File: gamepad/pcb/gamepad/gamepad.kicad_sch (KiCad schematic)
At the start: 11 parts, among them U1 Pico, U2 ADC, U3 RP2040-ZERO

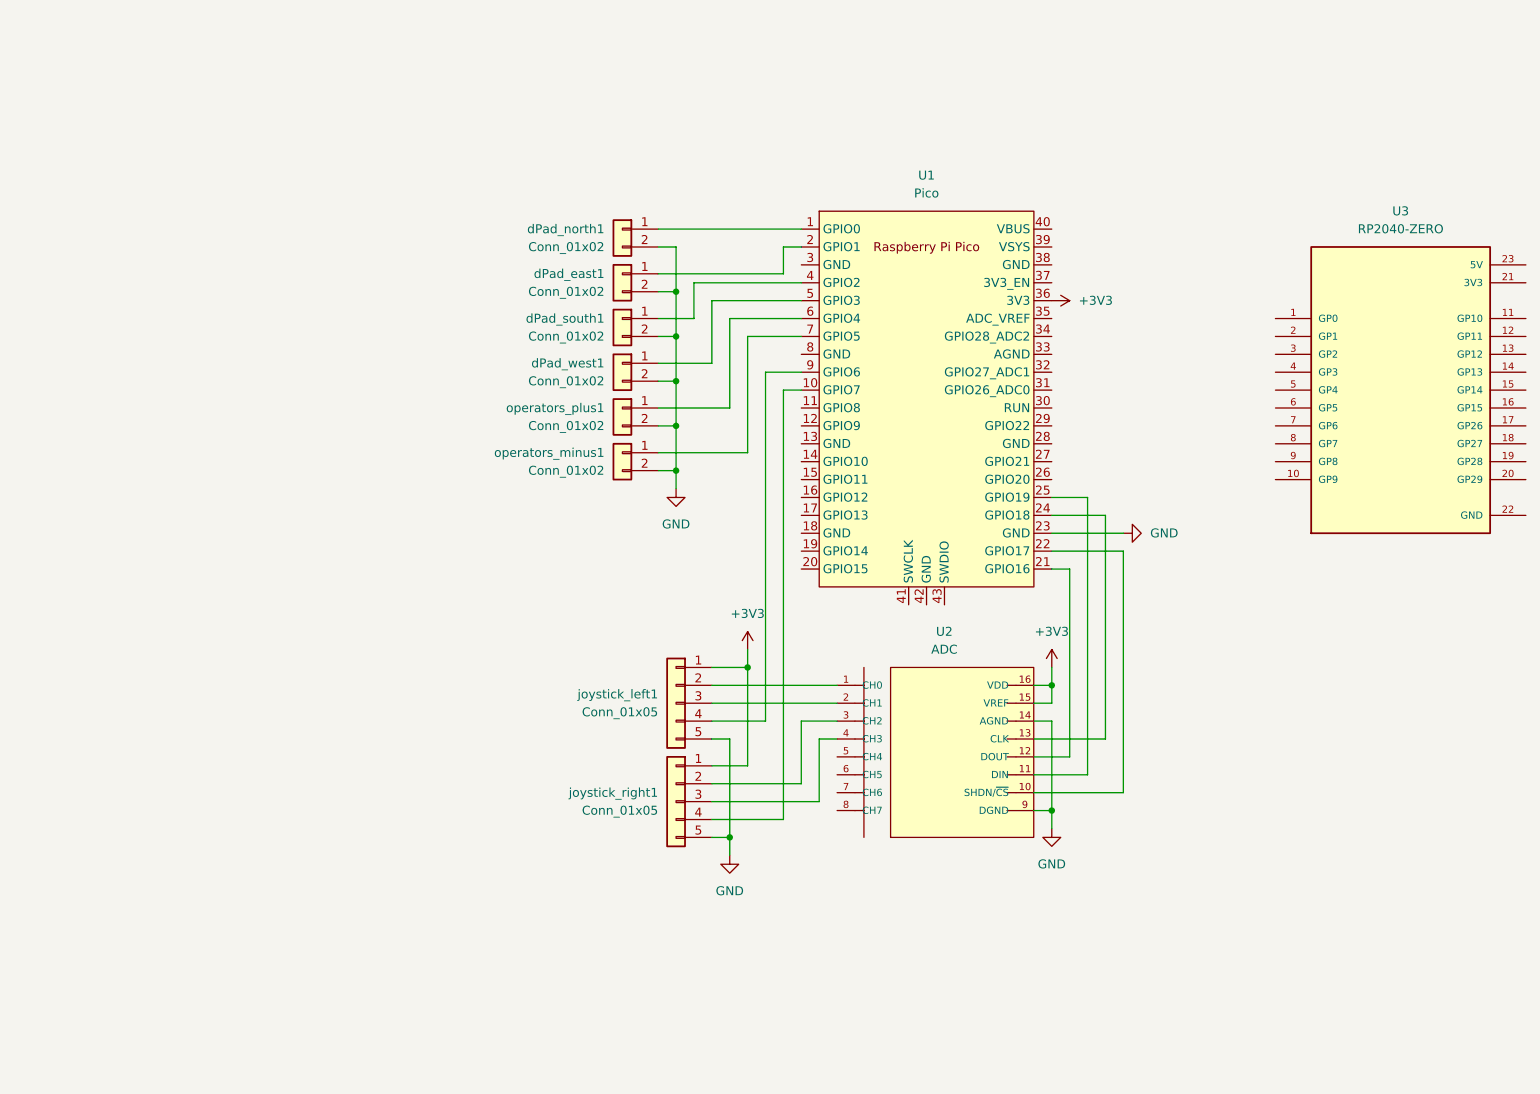
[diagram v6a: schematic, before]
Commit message: upt: pico to waveshare zero
change out the pcb to have a waveshare zero instead of a pico
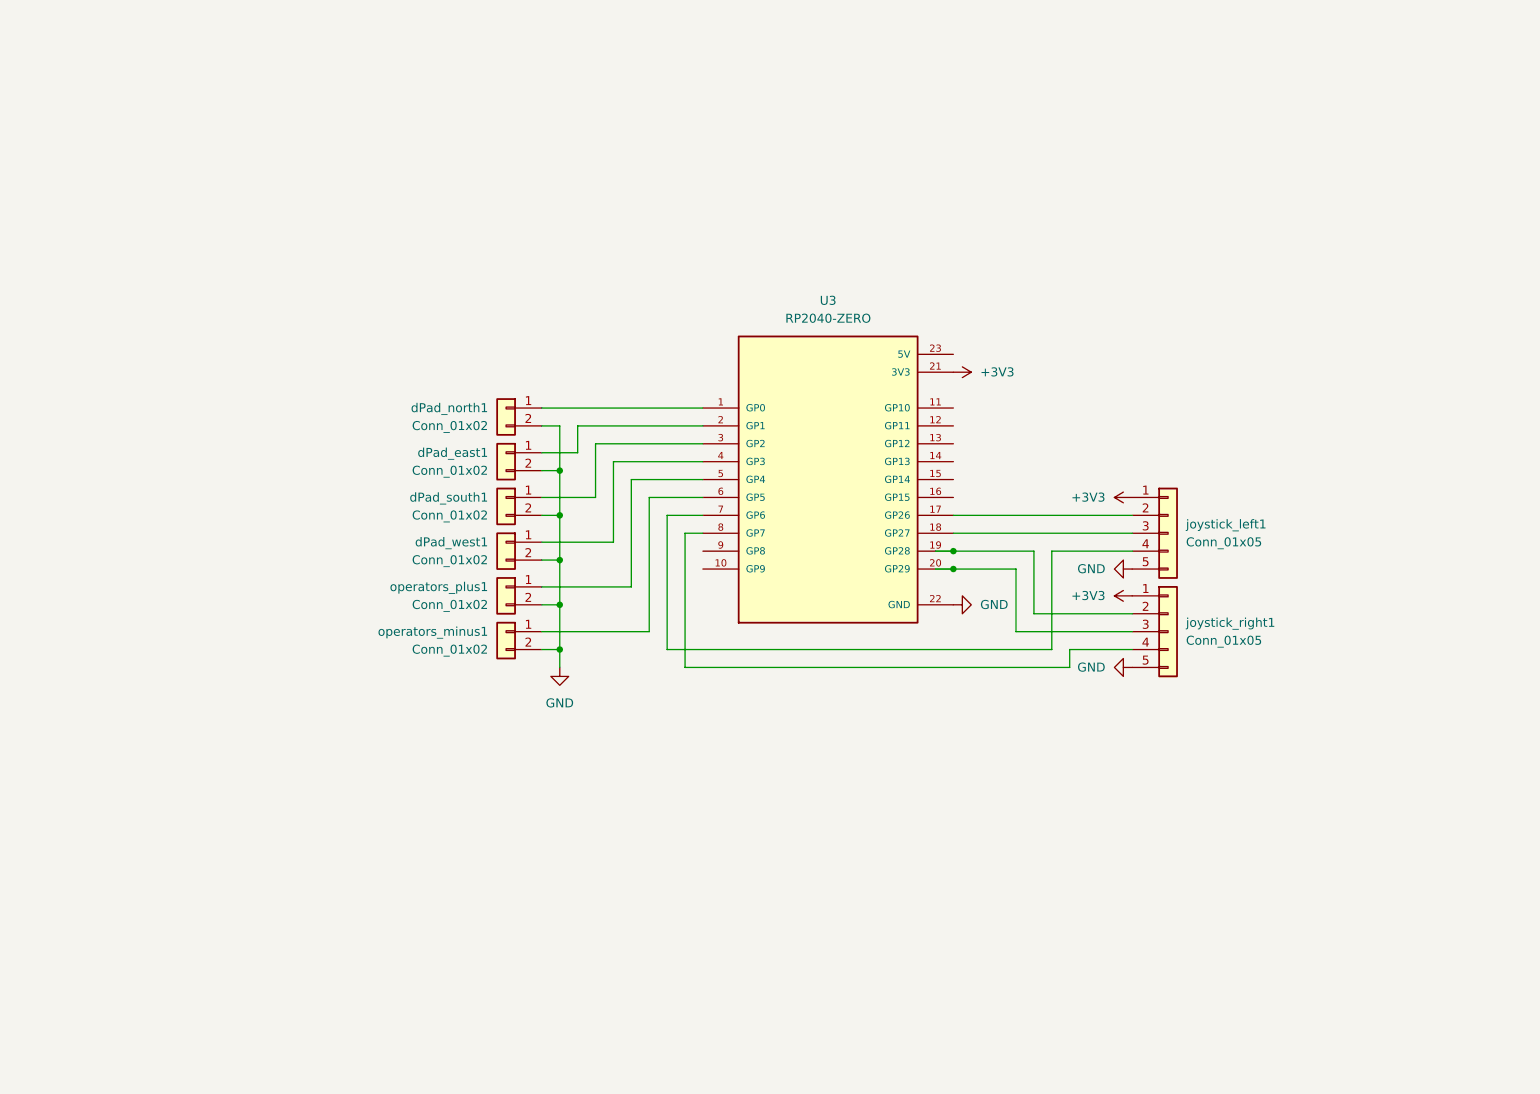
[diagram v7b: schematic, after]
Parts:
- removed U1: Pico, MCU_RaspberryPi_and_Boards:RPi_Pico_SMD_TH, symbol MCU_RaspberryPi_and_Boards:Pico
- removed U2: ADC, MCU-MCP3008:DIP16-2.54-19.2X7.62MM, symbol MCU-MCP3008-I_P_DIP16-7.62MM_:MCU-MCP3008-I_P_DIP16-7.62MM_
- dPad_east1, dPad_north1, dPad_south1, dPad_west1, operators_minus1, operators_plus1: footprint Connector_JST:JST_PH_B2B-PH-K_1x02_P2.00mm_Vertical -> Connector_JST:JST_XH_B2B-XH-A_1x02_P2.50mm_Vertical
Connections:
- net +3V3: now also U3.21 (3V3)
- net GND: now also U3.22 (GND)
- net at operators_plus1.1 (Pin_1): now also U3.5 (GP4)
- net at U3.1 (GP0): now also dPad_north1.1 (Pin_1)
- net at U3.17 (GP26): now also joystick_left1.2 (Pin_2)
- net at U3.18 (GP27): now also joystick_left1.3 (Pin_3)
- net at U3.19 (GP28): now also joystick_right1.2 (Pin_2)
- net at U3.2 (GP1): now also dPad_east1.1 (Pin_1)
- net at U3.20 (GP29): now also joystick_right1.3 (Pin_3)
- net at U3.3 (GP2): now also dPad_south1.1 (Pin_1)
- net at U3.4 (GP3): now also dPad_west1.1 (Pin_1)
- net at U3.6 (GP5): now also operators_minus1.1 (Pin_1)
- net at U3.7 (GP6): now also joystick_left1.4 (Pin_4)
- net at U3.8 (GP7): now also joystick_right1.4 (Pin_4)
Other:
- moved on the sheet: U3, dPad_east1, dPad_north1, dPad_south1, dPad_west1, joystick_left1, joystick_right1, operators_minus1, operators_plus1

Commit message: upt: pcb
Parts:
- added cardinal_down1, cardinal_left1, cardinal_right1, cardinal_up1: Conn_01x02, Connector_JST:JST_XH_B2B-XH-A_1x02_P2.50mm_Vertical, symbol Connector_Generic:Conn_01x02
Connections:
- net GND: now also cardinal_down1.2 (Pin_2), cardinal_left1.2 (Pin_2), cardinal_right1.2 (Pin_2), cardinal_up1.2 (Pin_2)
- net at operators_plus1.1 (Pin_1): now also U3.9 (GP8); no longer U3.5 (GP4)
- net at U3.10 (GP9): now also operators_minus1.1 (Pin_1)
- net at U3.11 (GP10): now also joystick_left1.4 (Pin_4)
- net at U3.12 (GP11): now also joystick_right1.4 (Pin_4)
- net at U3.6 (GP5): now also cardinal_right1.1 (Pin_1); no longer operators_minus1.1 (Pin_1)
- net at U3.7 (GP6): now also cardinal_down1.1 (Pin_1); no longer joystick_left1.4 (Pin_4)
- net at U3.8 (GP7): now also cardinal_left1.1 (Pin_1); no longer joystick_right1.4 (Pin_4)
- new net: U3.5 (GP4), cardinal_up1.1 (Pin_1)
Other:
- moved on the sheet: U3, dPad_east1, dPad_north1, dPad_south1, dPad_west1, joystick_left1, joystick_right1, operators_minus1, operators_plus1
